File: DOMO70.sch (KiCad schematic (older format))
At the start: 3 parts

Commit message: Layed down groundwork for schematic.
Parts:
- added SW? (x2): Rotary_Encoder_Switch, symbol Device:Rotary_Encoder_Switch
- added U?: OLED-SSD1306-OLED-SSD1306-4pin-128x32, symbol OLED-SSD1306-4pin-128x32:OLED-SSD1306-OLED-SSD1306-4pin-128x32
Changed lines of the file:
@@
 EESchema Schematic File Version 4
+LIBS:DOMO70-cache
 EELAYER 30 0
 EELAYER END
@@
 	1    0    0    -1
 $EndComp
+$Comp
+L OLED-SSD1306-4pin-128x32:OLED-SSD1306-OLED-SSD1306-4pin-128x32 U?
+U 1 1 5DFD98F6
+P 5700 4850
+F 0 "U?" H 5617 5225 50  0000 C CNN
+F 1 "OLED-SSD1306-OLED-SSD1306-4pin-128x32" H 5617 5134 50  0000 C CNN
+F 2 "" H 5700 5250 50  0001 C CNN
+F 3 "" H 5700 5250 50  0001 C CNN
+	1    5700 4850
+	1    0    0    -1
+$EndComp
+$Comp
+L Device:Rotary_Encoder_Switch SW?
+U 1 1 5DFDA3D1
+P 3750 3250
+F 0 "SW?" H 3750 3617 50  0000 C CNN
+F 1 "Rotary_Encoder_Switch" H 3750 3526 50  0000 C CNN
+F 2 "" H 3600 3410 50  0001 C CNN
+F 3 "~" H 3750 3510 50  0001 C CNN
+	1    3750 3250
+	1    0    0    -1
+$EndComp
+$Comp
+L Device:Rotary_Encoder_Switch SW?
+U 1 1 5DFDAD55
+P 4700 3300
+F 0 "SW?" H 4700 3667 50  0000 C CNN
+F 1 "Rotary_Encoder_Switch" H 4700 3576 50  0000 C CNN
+F 2 "" H 4550 3460 50  0001 C CNN
+F 3 "~" H 4700 3560 50  0001 C CNN
+	1    4700 3300
+	1    0    0    -1
+$EndComp

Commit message: First Real Schematic
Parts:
- added D10, D11, D12, D13, D14, D15, D16, D17, D18, D19, D2, D20, D21, D22, D23, D24, D25, D26, D27, D28, D29, D3, D30, D31, D32, D33, D34, D35, D36, D37, D38, D39, D4, D40, D41, D42, D43, D44, D45, D46, D47, D48, D49, D5, D50, D51, D52, D53, D54, D55, D56, D57, D58, D59, D6, D60, D61, D62, D63, D64, D65, D66, D67, D68, D69, D7, D70, D8, D9: 1N4148, Diode_THT:D_DO-35_SOD27_P7.62mm_Horizontal, symbol Diode:1N4148
- added MX10, MX11, MX12, MX13, MX14, MX15, MX16, MX17, MX18, MX19, MX2, MX20, MX21, MX22, MX23, MX24, MX25, MX26, MX27, MX28, MX29, MX3, MX30, MX31, MX32, MX33, MX34, MX35, MX36, MX37, MX38, MX39, MX4, MX40, MX41, MX42, MX43, MX44, MX45, MX46, MX47, MX48, MX49, MX5, MX50, MX51, MX52, MX53, MX54, MX55, MX56, MX57, MX58, MX59, MX6, MX60, MX61, MX62, MX63, MX64, MX65, MX66, MX67, MX68, MX69, MX7, MX70, MX8, MX9: MX-NoLED, symbol MX_Alps_Hybrid:MX-NoLED
- gave numbers to parts that had none: 6
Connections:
- net COL0: now reaches MX1.1 (COL)
- net COL0: now also U2.B11 (PB11), MX2.1 (COL), MX3.1 (COL), MX4.1 (COL), MX5.1 (COL), MX6.1 (COL), MX7.1 (COL), MX8.1 (COL), MX9.1 (COL)
- net at MX1.2 (ROW): now also D1.2 (A)
- net SDA: now reaches U1.1 (SDA)
- net SDA: now also U2.B7 (PB7/SDA)
- net SCL: now reaches U1.2 (SCL)
- net SCL: now also U2.B6 (PB6/SCL)
- net VCC: now reaches U1.3 (VCC)
- net VCC: now also U2.3.3V (VCC/3.3v)
- net GND: now reaches U1.4 (GND)
- net GND: now also SW1.C, SW2.C, U2.GND
- net ROW0: now reaches D1.1 (K)
- net ROW0: now also U2.A2 (PA2), D10.1 (K), D19.1 (K), D28.1 (K), D37.1 (K), D46.1 (K), D55.1 (K), D64.1 (K)
- net ENC1A: now reaches SW1.A
- net ENC1A: now also U2.B0 (PB0)
- net ENC1B: now reaches SW1.B
- net ENC1B: now also U2.B1 (PB1)
- net ROW7: now reaches SW1.S1
- net ROW7: now also U2.B9 (PB9), D17.1 (K), D26.1 (K), D35.1 (K), D44.1 (K), D53.1 (K), D62.1 (K), D8.1 (K)
- net COL7: now reaches SW1.S2
- net COL7: now also SW2.S2, U2.B2 (PB2), MX64.1 (COL), MX65.1 (COL), MX66.1 (COL), MX67.1 (COL), MX68.1 (COL), MX69.1 (COL), MX70.1 (COL)
- net ENC2A: now reaches SW2.A
- net ENC2A: now also U2.A7 (PA7)
- net ENC2B: now reaches SW2.B
- net ENC2B: now also U2.A6 (PA6)
- net ROW8: now reaches SW2.S1
- net ROW8: now also U2.B10 (PB10), D18.1 (K), D27.1 (K), D36.1 (K), D45.1 (K), D54.1 (K), D63.1 (K), D9.1 (K)
- net ROW2: now reaches U2.A0 (PA0)
- net ROW2: now also D12.1 (K), D21.1 (K), D3.1 (K), D30.1 (K), D39.1 (K), D48.1 (K), D57.1 (K), D66.1 (K)
- net ROW1: now reaches U2.A1 (PA1)
- net ROW1: now also D11.1 (K), D2.1 (K), D20.1 (K), D29.1 (K), D38.1 (K), D47.1 (K), D56.1 (K), D65.1 (K)
- net COL3: now reaches U2.A13 (PA13/SWDIO)
- net COL3: now also MX28.1 (COL), MX29.1 (COL), MX30.1 (COL), MX31.1 (COL), MX32.1 (COL), MX33.1 (COL), MX34.1 (COL), MX35.1 (COL), MX36.1 (COL)
- net COL2: now reaches U2.A14 (PA14/SWCLK)
- net COL2: now also MX19.1 (COL), MX20.1 (COL), MX21.1 (COL), MX22.1 (COL), MX23.1 (COL), MX24.1 (COL), MX25.1 (COL), MX26.1 (COL), MX27.1 (COL)
- net COL1: now reaches U2.B12 (PB12)
- net COL1: now also MX10.1 (COL), MX11.1 (COL), MX12.1 (COL), MX13.1 (COL), MX14.1 (COL), MX15.1 (COL), MX16.1 (COL), MX17.1 (COL), MX18.1 (COL)
- net ROW4: now reaches U2.B13 (PB13/SCLK)
- net ROW4: now also D14.1 (K), D23.1 (K), D32.1 (K), D41.1 (K), D5.1 (K), D50.1 (K), D59.1 (K), D68.1 (K)
- net ROW5: now reaches U2.B14 (PB14/MISO)
- net ROW5: now also D15.1 (K), D24.1 (K), D33.1 (K), D42.1 (K), D51.1 (K), D6.1 (K), D60.1 (K), D69.1 (K)
- net ROW6: now reaches U2.B15 (PB15/MOSI)
- net ROW6: now also D16.1 (K), D25.1 (K), D34.1 (K), D43.1 (K), D52.1 (K), D61.1 (K), D7.1 (K), D70.1 (K)
- net COL6: now reaches U2.B3 (PB3)
- net COL6: now also MX55.1 (COL), MX56.1 (COL), MX57.1 (COL), MX58.1 (COL), MX59.1 (COL), MX60.1 (COL), MX61.1 (COL), MX62.1 (COL), MX63.1 (COL)
- net COL5: now reaches U2.B4 (PB4)
- net COL5: now also MX46.1 (COL), MX47.1 (COL), MX48.1 (COL), MX49.1 (COL), MX50.1 (COL), MX51.1 (COL), MX52.1 (COL), MX53.1 (COL), MX54.1 (COL)
- net COL4: now reaches U2.B5 (PB5)
- net COL4: now also MX37.1 (COL), MX38.1 (COL), MX39.1 (COL), MX40.1 (COL), MX41.1 (COL), MX42.1 (COL), MX43.1 (COL), MX44.1 (COL), MX45.1 (COL)
- net ROW3: now reaches U2.B8 (PB8)
- net ROW3: now also D13.1 (K), D22.1 (K), D31.1 (K), D4.1 (K), D40.1 (K), D49.1 (K), D58.1 (K), D67.1 (K)
- new net: D10.2 (A), MX10.2 (ROW)
- new net: D2.2 (A), MX2.2 (ROW)
- new net: D11.2 (A), MX11.2 (ROW)
- new net: D19.2 (A), MX19.2 (ROW)
- new net: D28.2 (A), MX28.2 (ROW)
- new net: D20.2 (A), MX20.2 (ROW)
- new net: D29.2 (A), MX29.2 (ROW)
- new net: D3.2 (A), MX3.2 (ROW)
- new net: D12.2 (A), MX12.2 (ROW)
- new net: D4.2 (A), MX4.2 (ROW)
- new net: D13.2 (A), MX13.2 (ROW)
- new net: D21.2 (A), MX21.2 (ROW)
- new net: D30.2 (A), MX30.2 (ROW)
- new net: D22.2 (A), MX22.2 (ROW)
- new net: D31.2 (A), MX31.2 (ROW)
- new net: D5.2 (A), MX5.2 (ROW)
- new net: D14.2 (A), MX14.2 (ROW)
- new net: D23.2 (A), MX23.2 (ROW)
- new net: D32.2 (A), MX32.2 (ROW)
- new net: D37.2 (A), MX37.2 (ROW)
- new net: D46.2 (A), MX46.2 (ROW)
- new net: D38.2 (A), MX38.2 (ROW)
- new net: D47.2 (A), MX47.2 (ROW)
- new net: D55.2 (A), MX55.2 (ROW)
- new net: D64.2 (A), MX64.2 (ROW)
- new net: D56.2 (A), MX56.2 (ROW)
- new net: D65.2 (A), MX65.2 (ROW)
- new net: D39.2 (A), MX39.2 (ROW)
- new net: D48.2 (A), MX48.2 (ROW)
- new net: D40.2 (A), MX40.2 (ROW)
- new net: D49.2 (A), MX49.2 (ROW)
- new net: D57.2 (A), MX57.2 (ROW)
- new net: D66.2 (A), MX66.2 (ROW)
- new net: D58.2 (A), MX58.2 (ROW)
- new net: D67.2 (A), MX67.2 (ROW)
- new net: D41.2 (A), MX41.2 (ROW)
- new net: D50.2 (A), MX50.2 (ROW)
- new net: D59.2 (A), MX59.2 (ROW)
- new net: D68.2 (A), MX68.2 (ROW)
- new net: D6.2 (A), MX6.2 (ROW)
- new net: D15.2 (A), MX15.2 (ROW)
- new net: D7.2 (A), MX7.2 (ROW)
- new net: D16.2 (A), MX16.2 (ROW)
- new net: D24.2 (A), MX24.2 (ROW)
- new net: D33.2 (A), MX33.2 (ROW)
- new net: D25.2 (A), MX25.2 (ROW)
- new net: D34.2 (A), MX34.2 (ROW)
- new net: D8.2 (A), MX8.2 (ROW)
- new net: D17.2 (A), MX17.2 (ROW)
- new net: D9.2 (A), MX9.2 (ROW)
- new net: D18.2 (A), MX18.2 (ROW)
- new net: D26.2 (A), MX26.2 (ROW)
- new net: D35.2 (A), MX35.2 (ROW)
- new net: D27.2 (A), MX27.2 (ROW)
- new net: D36.2 (A), MX36.2 (ROW)
- new net: D42.2 (A), MX42.2 (ROW)
- new net: D51.2 (A), MX51.2 (ROW)
- new net: D43.2 (A), MX43.2 (ROW)
- new net: D52.2 (A), MX52.2 (ROW)
- new net: D60.2 (A), MX60.2 (ROW)
- new net: D61.2 (A), MX61.2 (ROW)
- new net: D69.2 (A), MX69.2 (ROW)
- new net: D44.2 (A), MX44.2 (ROW)
- new net: D53.2 (A), MX53.2 (ROW)
- new net: D45.2 (A), MX45.2 (ROW)
- new net: D54.2 (A), MX54.2 (ROW)
- new net: D62.2 (A), MX62.2 (ROW)
- new net: D70.2 (A), MX70.2 (ROW)
- new net: D63.2 (A), MX63.2 (ROW)
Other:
- moved on the sheet: D1, MX1, SW1, SW2, U1, U2

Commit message: Messing with matrix
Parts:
- removed D53: 1N4148, Diode_THT:D_DO-35_SOD27_P7.62mm_Horizontal, symbol Diode:1N4148
- removed MX53: MX-NoLED, symbol MX_Alps_Hybrid:MX-NoLED
- added D? (x5): 1N4148, cftkb:D_DO-35_SOD27_P5.08mm_Horizontal, symbol Diode:1N4148
- added MX? (x3): MX-NoLED, MX_Only:MXOnly-1U-NoLED, symbol MX_Alps_Hybrid:MX-NoLED
- D?: renamed from D1; footprint Diode_THT:D_DO-35_SOD27_P7.62mm_Horizontal -> cftkb:D_DO-35_SOD27_P5.08mm_Horizontal
- D?: renamed from D10; footprint Diode_THT:D_DO-35_SOD27_P7.62mm_Horizontal -> cftkb:D_DO-35_SOD27_P5.08mm_Horizontal
- D?: renamed from D2; footprint Diode_THT:D_DO-35_SOD27_P7.62mm_Horizontal -> cftkb:D_DO-35_SOD27_P5.08mm_Horizontal
- D?: renamed from D11; footprint Diode_THT:D_DO-35_SOD27_P7.62mm_Horizontal -> cftkb:D_DO-35_SOD27_P5.08mm_Horizontal
- D?: renamed from D19; footprint Diode_THT:D_DO-35_SOD27_P7.62mm_Horizontal -> cftkb:D_DO-35_SOD27_P5.08mm_Horizontal
- D?: renamed from D28; footprint Diode_THT:D_DO-35_SOD27_P7.62mm_Horizontal -> cftkb:D_DO-35_SOD27_P5.08mm_Horizontal
- D?: renamed from D20; footprint Diode_THT:D_DO-35_SOD27_P7.62mm_Horizontal -> cftkb:D_DO-35_SOD27_P5.08mm_Horizontal
- D?: renamed from D29; footprint Diode_THT:D_DO-35_SOD27_P7.62mm_Horizontal -> cftkb:D_DO-35_SOD27_P5.08mm_Horizontal
- D?: renamed from D3; footprint Diode_THT:D_DO-35_SOD27_P7.62mm_Horizontal -> cftkb:D_DO-35_SOD27_P5.08mm_Horizontal
- D?: renamed from D12; footprint Diode_THT:D_DO-35_SOD27_P7.62mm_Horizontal -> cftkb:D_DO-35_SOD27_P5.08mm_Horizontal
- D?: renamed from D4; footprint Diode_THT:D_DO-35_SOD27_P7.62mm_Horizontal -> cftkb:D_DO-35_SOD27_P5.08mm_Horizontal
- D?: renamed from D13; footprint Diode_THT:D_DO-35_SOD27_P7.62mm_Horizontal -> cftkb:D_DO-35_SOD27_P5.08mm_Horizontal
- D?: renamed from D21; footprint Diode_THT:D_DO-35_SOD27_P7.62mm_Horizontal -> cftkb:D_DO-35_SOD27_P5.08mm_Horizontal
- D?: renamed from D30; footprint Diode_THT:D_DO-35_SOD27_P7.62mm_Horizontal -> cftkb:D_DO-35_SOD27_P5.08mm_Horizontal
- D?: renamed from D22; footprint Diode_THT:D_DO-35_SOD27_P7.62mm_Horizontal -> cftkb:D_DO-35_SOD27_P5.08mm_Horizontal
- D?: renamed from D31; footprint Diode_THT:D_DO-35_SOD27_P7.62mm_Horizontal -> cftkb:D_DO-35_SOD27_P5.08mm_Horizontal
- D?: renamed from D5; footprint Diode_THT:D_DO-35_SOD27_P7.62mm_Horizontal -> cftkb:D_DO-35_SOD27_P5.08mm_Horizontal
- D?: renamed from D14; footprint Diode_THT:D_DO-35_SOD27_P7.62mm_Horizontal -> cftkb:D_DO-35_SOD27_P5.08mm_Horizontal
- D?: renamed from D23; footprint Diode_THT:D_DO-35_SOD27_P7.62mm_Horizontal -> cftkb:D_DO-35_SOD27_P5.08mm_Horizontal
- D?: renamed from D32; footprint Diode_THT:D_DO-35_SOD27_P7.62mm_Horizontal -> cftkb:D_DO-35_SOD27_P5.08mm_Horizontal
- D?: renamed from D37; footprint Diode_THT:D_DO-35_SOD27_P7.62mm_Horizontal -> cftkb:D_DO-35_SOD27_P5.08mm_Horizontal
- D?: renamed from D46; footprint Diode_THT:D_DO-35_SOD27_P7.62mm_Horizontal -> cftkb:D_DO-35_SOD27_P5.08mm_Horizontal
- D?: renamed from D38; footprint Diode_THT:D_DO-35_SOD27_P7.62mm_Horizontal -> cftkb:D_DO-35_SOD27_P5.08mm_Horizontal
- D?: renamed from D47; footprint Diode_THT:D_DO-35_SOD27_P7.62mm_Horizontal -> cftkb:D_DO-35_SOD27_P5.08mm_Horizontal
- D?: renamed from D55; footprint Diode_THT:D_DO-35_SOD27_P7.62mm_Horizontal -> cftkb:D_DO-35_SOD27_P5.08mm_Horizontal
- D?: renamed from D64; footprint Diode_THT:D_DO-35_SOD27_P7.62mm_Horizontal -> cftkb:D_DO-35_SOD27_P5.08mm_Horizontal
- D?: renamed from D56; footprint Diode_THT:D_DO-35_SOD27_P7.62mm_Horizontal -> cftkb:D_DO-35_SOD27_P5.08mm_Horizontal
- D?: renamed from D65; footprint Diode_THT:D_DO-35_SOD27_P7.62mm_Horizontal -> cftkb:D_DO-35_SOD27_P5.08mm_Horizontal
- D?: renamed from D39; footprint Diode_THT:D_DO-35_SOD27_P7.62mm_Horizontal -> cftkb:D_DO-35_SOD27_P5.08mm_Horizontal
- D?: renamed from D48; footprint Diode_THT:D_DO-35_SOD27_P7.62mm_Horizontal -> cftkb:D_DO-35_SOD27_P5.08mm_Horizontal
- D?: renamed from D40; footprint Diode_THT:D_DO-35_SOD27_P7.62mm_Horizontal -> cftkb:D_DO-35_SOD27_P5.08mm_Horizontal
- D?: renamed from D49; footprint Diode_THT:D_DO-35_SOD27_P7.62mm_Horizontal -> cftkb:D_DO-35_SOD27_P5.08mm_Horizontal
- D?: renamed from D57; footprint Diode_THT:D_DO-35_SOD27_P7.62mm_Horizontal -> cftkb:D_DO-35_SOD27_P5.08mm_Horizontal
- D?: renamed from D66; footprint Diode_THT:D_DO-35_SOD27_P7.62mm_Horizontal -> cftkb:D_DO-35_SOD27_P5.08mm_Horizontal
- D?: renamed from D58; footprint Diode_THT:D_DO-35_SOD27_P7.62mm_Horizontal -> cftkb:D_DO-35_SOD27_P5.08mm_Horizontal
- D?: renamed from D67; footprint Diode_THT:D_DO-35_SOD27_P7.62mm_Horizontal -> cftkb:D_DO-35_SOD27_P5.08mm_Horizontal
- D?: renamed from D41; footprint Diode_THT:D_DO-35_SOD27_P7.62mm_Horizontal -> cftkb:D_DO-35_SOD27_P5.08mm_Horizontal
- D?: renamed from D50; footprint Diode_THT:D_DO-35_SOD27_P7.62mm_Horizontal -> cftkb:D_DO-35_SOD27_P5.08mm_Horizontal
- D?: renamed from D59; footprint Diode_THT:D_DO-35_SOD27_P7.62mm_Horizontal -> cftkb:D_DO-35_SOD27_P5.08mm_Horizontal
- D?: renamed from D68; footprint Diode_THT:D_DO-35_SOD27_P7.62mm_Horizontal -> cftkb:D_DO-35_SOD27_P5.08mm_Horizontal
- D?: renamed from D6; footprint Diode_THT:D_DO-35_SOD27_P7.62mm_Horizontal -> cftkb:D_DO-35_SOD27_P5.08mm_Horizontal
- D?: renamed from D15; footprint Diode_THT:D_DO-35_SOD27_P7.62mm_Horizontal -> cftkb:D_DO-35_SOD27_P5.08mm_Horizontal
- D?: renamed from D7; footprint Diode_THT:D_DO-35_SOD27_P7.62mm_Horizontal -> cftkb:D_DO-35_SOD27_P5.08mm_Horizontal
- D?: renamed from D16; footprint Diode_THT:D_DO-35_SOD27_P7.62mm_Horizontal -> cftkb:D_DO-35_SOD27_P5.08mm_Horizontal
- D?: renamed from D24; footprint Diode_THT:D_DO-35_SOD27_P7.62mm_Horizontal -> cftkb:D_DO-35_SOD27_P5.08mm_Horizontal
- D?: renamed from D33; footprint Diode_THT:D_DO-35_SOD27_P7.62mm_Horizontal -> cftkb:D_DO-35_SOD27_P5.08mm_Horizontal
- D?: renamed from D25; footprint Diode_THT:D_DO-35_SOD27_P7.62mm_Horizontal -> cftkb:D_DO-35_SOD27_P5.08mm_Horizontal
- D?: renamed from D34; footprint Diode_THT:D_DO-35_SOD27_P7.62mm_Horizontal -> cftkb:D_DO-35_SOD27_P5.08mm_Horizontal
- D?: renamed from D8; footprint Diode_THT:D_DO-35_SOD27_P7.62mm_Horizontal -> cftkb:D_DO-35_SOD27_P5.08mm_Horizontal
- D?: renamed from D17; footprint Diode_THT:D_DO-35_SOD27_P7.62mm_Horizontal -> cftkb:D_DO-35_SOD27_P5.08mm_Horizontal
- D?: renamed from D9; footprint Diode_THT:D_DO-35_SOD27_P7.62mm_Horizontal -> cftkb:D_DO-35_SOD27_P5.08mm_Horizontal
- D?: renamed from D18; footprint Diode_THT:D_DO-35_SOD27_P7.62mm_Horizontal -> cftkb:D_DO-35_SOD27_P5.08mm_Horizontal
- D?: renamed from D26; footprint Diode_THT:D_DO-35_SOD27_P7.62mm_Horizontal -> cftkb:D_DO-35_SOD27_P5.08mm_Horizontal
- D?: renamed from D35; footprint Diode_THT:D_DO-35_SOD27_P7.62mm_Horizontal -> cftkb:D_DO-35_SOD27_P5.08mm_Horizontal
- D?: renamed from D27; footprint Diode_THT:D_DO-35_SOD27_P7.62mm_Horizontal -> cftkb:D_DO-35_SOD27_P5.08mm_Horizontal
- D?: renamed from D36; footprint Diode_THT:D_DO-35_SOD27_P7.62mm_Horizontal -> cftkb:D_DO-35_SOD27_P5.08mm_Horizontal
- D?: renamed from D42; footprint Diode_THT:D_DO-35_SOD27_P7.62mm_Horizontal -> cftkb:D_DO-35_SOD27_P5.08mm_Horizontal
- D?: renamed from D51; footprint Diode_THT:D_DO-35_SOD27_P7.62mm_Horizontal -> cftkb:D_DO-35_SOD27_P5.08mm_Horizontal
- D?: renamed from D43; footprint Diode_THT:D_DO-35_SOD27_P7.62mm_Horizontal -> cftkb:D_DO-35_SOD27_P5.08mm_Horizontal
- D?: renamed from D52; footprint Diode_THT:D_DO-35_SOD27_P7.62mm_Horizontal -> cftkb:D_DO-35_SOD27_P5.08mm_Horizontal
- D?: renamed from D60; footprint Diode_THT:D_DO-35_SOD27_P7.62mm_Horizontal -> cftkb:D_DO-35_SOD27_P5.08mm_Horizontal
- D?: renamed from D61; footprint Diode_THT:D_DO-35_SOD27_P7.62mm_Horizontal -> cftkb:D_DO-35_SOD27_P5.08mm_Horizontal
- D?: renamed from D69; footprint Diode_THT:D_DO-35_SOD27_P7.62mm_Horizontal -> cftkb:D_DO-35_SOD27_P5.08mm_Horizontal
- D?: renamed from D44; footprint Diode_THT:D_DO-35_SOD27_P7.62mm_Horizontal -> cftkb:D_DO-35_SOD27_P5.08mm_Horizontal
- D?: renamed from D45; footprint Diode_THT:D_DO-35_SOD27_P7.62mm_Horizontal -> cftkb:D_DO-35_SOD27_P5.08mm_Horizontal
- D?: renamed from D54; footprint Diode_THT:D_DO-35_SOD27_P7.62mm_Horizontal -> cftkb:D_DO-35_SOD27_P5.08mm_Horizontal
- D?: renamed from D62; footprint Diode_THT:D_DO-35_SOD27_P7.62mm_Horizontal -> cftkb:D_DO-35_SOD27_P5.08mm_Horizontal
- D?: renamed from D70; footprint Diode_THT:D_DO-35_SOD27_P7.62mm_Horizontal -> cftkb:D_DO-35_SOD27_P5.08mm_Horizontal
- D?: renamed from D63; footprint Diode_THT:D_DO-35_SOD27_P7.62mm_Horizontal -> cftkb:D_DO-35_SOD27_P5.08mm_Horizontal
- MX?: renamed from MX1; footprint (none) -> MX_Only:MXOnly-1U-NoLED
- MX?: renamed from MX10; footprint (none) -> MX_Only:MXOnly-1U-NoLED
- MX?: renamed from MX2; footprint (none) -> MX_Only:MXOnly-1.5U-NoLED
- MX?: renamed from MX11; footprint (none) -> MX_Only:MXOnly-1U-NoLED
- MX?: renamed from MX19; footprint (none) -> MX_Only:MXOnly-1U-NoLED
- MX?: renamed from MX28; footprint (none) -> MX_Only:MXOnly-1U-NoLED
- MX?: renamed from MX20; footprint (none) -> MX_Only:MXOnly-1U-NoLED
- MX?: renamed from MX29; footprint (none) -> MX_Only:MXOnly-1U-NoLED
- MX?: renamed from MX3; footprint (none) -> MX_Only:MXOnly-1U-NoLED
- MX?: renamed from MX12; footprint (none) -> MX_Only:MXOnly-1U-NoLED
- MX?: renamed from MX4; footprint (none) -> MX_Only:MXOnly-1U-NoLED
- MX?: renamed from MX13; footprint (none) -> MX_Only:MXOnly-1U-NoLED
- MX?: renamed from MX21; footprint (none) -> MX_Only:MXOnly-1U-NoLED
- MX?: renamed from MX30; footprint (none) -> MX_Only:MXOnly-1U-NoLED
- MX?: renamed from MX22; footprint (none) -> MX_Only:MXOnly-1U-NoLED
- MX?: renamed from MX31; footprint (none) -> MX_Only:MXOnly-1U-NoLED
- MX?: renamed from MX5; footprint (none) -> MX_Only:MXOnly-1U-NoLED
- MX?: renamed from MX14; footprint (none) -> MX_Only:MXOnly-1U-NoLED
- MX?: renamed from MX23; footprint (none) -> MX_Only:MXOnly-1U-NoLED
- MX?: renamed from MX32; footprint (none) -> MX_Only:MXOnly-1U-NoLED
- MX?: renamed from MX37; footprint (none) -> MX_Only:MXOnly-1U-NoLED
- MX?: renamed from MX46; footprint (none) -> MX_Only:MXOnly-1U-NoLED
- MX?: renamed from MX38; footprint (none) -> MX_Only:MXOnly-1U-NoLED
- MX?: renamed from MX47; footprint (none) -> MX_Only:MXOnly-1U-NoLED
- MX?: renamed from MX55; footprint (none) -> MX_Only:MXOnly-1U-NoLED
- MX?: renamed from MX64; footprint (none) -> MX_Only:MXOnly-1U-NoLED
- MX?: renamed from MX56; footprint (none) -> MX_Only:MXOnly-1U-NoLED
- MX?: renamed from MX65; footprint (none) -> MX_Only:MXOnly-1U-NoLED
- MX?: renamed from MX39; footprint (none) -> MX_Only:MXOnly-1U-NoLED
- MX?: renamed from MX48; footprint (none) -> MX_Only:MXOnly-1U-NoLED
- MX?: renamed from MX40; footprint (none) -> MX_Only:MXOnly-1U-NoLED
- MX?: renamed from MX49; footprint (none) -> MX_Only:MXOnly-1U-NoLED
- MX?: renamed from MX57; footprint (none) -> MX_Only:MXOnly-1U-NoLED
- MX?: renamed from MX66; footprint (none) -> MX_Only:MXOnly-1U-NoLED
- MX?: renamed from MX58; footprint (none) -> MX_Only:MXOnly-1U-NoLED
- MX?: renamed from MX67; footprint (none) -> MX_Only:MXOnly-1U-NoLED
- MX?: renamed from MX41; footprint (none) -> MX_Only:MXOnly-1U-NoLED
- MX?: renamed from MX50; footprint (none) -> MX_Only:MXOnly-1U-NoLED
- MX?: renamed from MX59; footprint (none) -> MX_Only:MXOnly-1U-NoLED
- MX?: renamed from MX68; footprint (none) -> MX_Only:MXOnly-1U-NoLED
- MX?: renamed from MX6; footprint (none) -> MX_Only:MXOnly-1U-NoLED
- MX?: renamed from MX15; footprint (none) -> MX_Only:MXOnly-1U-NoLED
- MX?: renamed from MX7; footprint (none) -> MX_Only:MXOnly-1U-NoLED
- MX?: renamed from MX16; footprint (none) -> MX_Only:MXOnly-1U-NoLED
- MX?: renamed from MX24; footprint (none) -> MX_Only:MXOnly-1U-NoLED
- MX?: renamed from MX33; footprint (none) -> MX_Only:MXOnly-1U-NoLED
- MX?: renamed from MX25; footprint (none) -> MX_Only:MXOnly-1U-NoLED
- MX?: renamed from MX34; footprint (none) -> MX_Only:MXOnly-1U-NoLED
- MX?: renamed from MX8; footprint (none) -> MX_Only:MXOnly-1U-NoLED
- MX?: renamed from MX17; footprint (none) -> MX_Only:MXOnly-1U-NoLED
- MX?: renamed from MX9; footprint (none) -> MX_Only:MXOnly-1U-NoLED
- MX?: renamed from MX18; footprint (none) -> MX_Only:MXOnly-1U-NoLED
- MX?: renamed from MX26; footprint (none) -> MX_Only:MXOnly-1U-NoLED
- MX?: renamed from MX35; footprint (none) -> MX_Only:MXOnly-1U-NoLED
- MX?: renamed from MX27; footprint (none) -> MX_Only:MXOnly-1U-NoLED
- MX?: renamed from MX36; footprint (none) -> MX_Only:MXOnly-1U-NoLED
- MX?: renamed from MX42; footprint (none) -> MX_Only:MXOnly-1U-NoLED
- MX?: renamed from MX51; footprint (none) -> MX_Only:MXOnly-1U-NoLED
- MX?: renamed from MX43; footprint (none) -> MX_Only:MXOnly-1U-NoLED
- MX?: renamed from MX52; footprint (none) -> MX_Only:MXOnly-1U-NoLED
- MX?: renamed from MX60; footprint (none) -> MX_Only:MXOnly-1U-NoLED
- MX?: renamed from MX61; footprint (none) -> MX_Only:MXOnly-1U-NoLED
- MX?: renamed from MX69; footprint (none) -> MX_Only:MXOnly-1U-NoLED
- MX?: renamed from MX44; footprint (none) -> MX_Only:MXOnly-1U-NoLED
- MX?: renamed from MX45; footprint (none) -> MX_Only:MXOnly-1U-NoLED
- MX?: renamed from MX54; footprint (none) -> MX_Only:MXOnly-1U-NoLED
- MX?: renamed from MX62; footprint (none) -> MX_Only:MXOnly-1U-NoLED
- MX?: renamed from MX70; footprint (none) -> MX_Only:MXOnly-1U-NoLED
- MX?: renamed from MX63; footprint (none) -> MX_Only:MXOnly-1U-NoLED
- SW?: renamed from SW1; footprint (none) -> Rotary_Encoder:RotaryEncoder_Alps_EC11E-Switch_Vertical_H20mm
- SW?: renamed from SW2; footprint (none) -> Rotary_Encoder:RotaryEncoder_Alps_EC11E-Switch_Vertical_H20mm
- U?: renamed from U1; footprint (none) -> OLED-SSD1306-4pin-128x32:OLED-1306-Supports
- U?: renamed from U2; footprint (none) -> proton_c:proton_c
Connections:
- net COL0: now also U?.B14 (PB14/MISO); no longer MX?.1 (COL), MX?.1 (COL), MX?.1 (COL), MX?.1 (COL), U?.B11 (PB11)
- net COL1: now also U?.B15 (PB15/MOSI); no longer MX?.1 (COL), MX?.1 (COL), MX?.1 (COL), MX?.1 (COL), U?.B12 (PB12)
- net COL2: now also U?.B9 (PB9); no longer MX?.1 (COL), MX?.1 (COL), MX?.1 (COL), MX?.1 (COL), U?.A14 (PA14/SWCLK)
- net COL3: now also U?.B10 (PB10); no longer MX?.1 (COL), MX?.1 (COL), MX?.1 (COL), MX?.1 (COL), U?.A13 (PA13/SWDIO)
- net COL4: now also MX?.1 (COL), U?.B11 (PB11); no longer MX?.1 (COL), MX?.1 (COL), MX?.1 (COL), MX?.1 (COL), MX?.1 (COL), U?.B5 (PB5)
- net COL5: now also MX?.1 (COL), U?.B12 (PB12); no longer MX?.1 (COL), MX?.1 (COL), MX?.1 (COL), MX?.1 (COL), U?.B4 (PB4)
- net COL6: now also MX?.1 (COL), U?.A14 (PA14/SWCLK); no longer MX?.1 (COL), MX?.1 (COL), MX?.1 (COL), MX?.1 (COL), MX?.1 (COL), U?.B3 (PB3)
- net COL7: now also U?.A13 (PA13/SWDIO); no longer MX?.1 (COL), MX?.1 (COL), MX?.1 (COL), SW?.S2, SW?.S2, U?.B2 (PB2)
- net ROW0: now also D?.1 (K), D?.1 (K), D?.1 (K), D?.1 (K), D?.1 (K), D?.1 (K), D?.1 (K)
- net ROW1: now also D?.1 (K), D?.1 (K), D?.1 (K), D?.1 (K), D?.1 (K), D?.1 (K)
- net ROW2: now also D?.1 (K), D?.1 (K), D?.1 (K), D?.1 (K), D?.1 (K)
- net ROW3: now also D?.1 (K), D?.1 (K), D?.1 (K), D?.1 (K), D?.1 (K)
- net ROW4: now also D?.1 (K), D?.1 (K), D?.1 (K), D?.1 (K); no longer D?.1 (K)
- net COL13: now reaches U?.A10 (PA10/RX)
- net COL13: now also MX?.1 (COL), MX?.1 (COL), MX?.1 (COL)
- net COL8: now reaches U?.A8 (PA8)
- net COL8: now also MX?.1 (COL), MX?.1 (COL), MX?.1 (COL), MX?.1 (COL)
- net COL14: now reaches U?.A9 (PA9/TX)
- net COL14: now also MX?.1 (COL), MX?.1 (COL), MX?.1 (COL), MX?.1 (COL)
- removed net ROW5: D?.1 (K), D?.1 (K), D?.1 (K), D?.1 (K), D?.1 (K), D?.1 (K), D?.1 (K), D?.1 (K), U?.B14 (PB14/MISO)
- removed net ROW6: D?.1 (K), D?.1 (K), D?.1 (K), D?.1 (K), D?.1 (K), D?.1 (K), D?.1 (K), D?.1 (K), U?.B15 (PB15/MOSI)
- removed net ROW7: D?.1 (K), D?.1 (K), D?.1 (K), D?.1 (K), D?.1 (K), D?.1 (K), SW?.S1, U?.B9 (PB9)
- removed net ROW8: D?.1 (K), D?.1 (K), D?.1 (K), D?.1 (K), D?.1 (K), D?.1 (K), D?.1 (K), SW?.S1, U?.B10 (PB10)
- new net: D?.2 (A), SW?.S1 (x2)
- new net: MX?.1 (COL), MX?.1 (COL) (x3)
- new net: D?.1 (K), D?.1 (K), D?.1 (K) (x2)
- new net: D?.2 (A), MX?.2 (ROW) (x3)
- new net COL10: MX?.1 (COL), MX?.1 (COL), MX?.1 (COL), MX?.1 (COL), MX?.1 (COL), U?.B3 (PB3)
- new net COL11: MX?.1 (COL), MX?.1 (COL), MX?.1 (COL), MX?.1 (COL), U?.B4 (PB4)
- new net COL12: MX?.1 (COL), MX?.1 (COL), MX?.1 (COL), U?.B5 (PB5)
- new net COL9: MX?.1 (COL), MX?.1 (COL), MX?.1 (COL), MX?.1 (COL), U?.B2 (PB2)
- no-connect marks 0 -> 5
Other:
- moved on the sheet: D?, MX?, SW?, U?

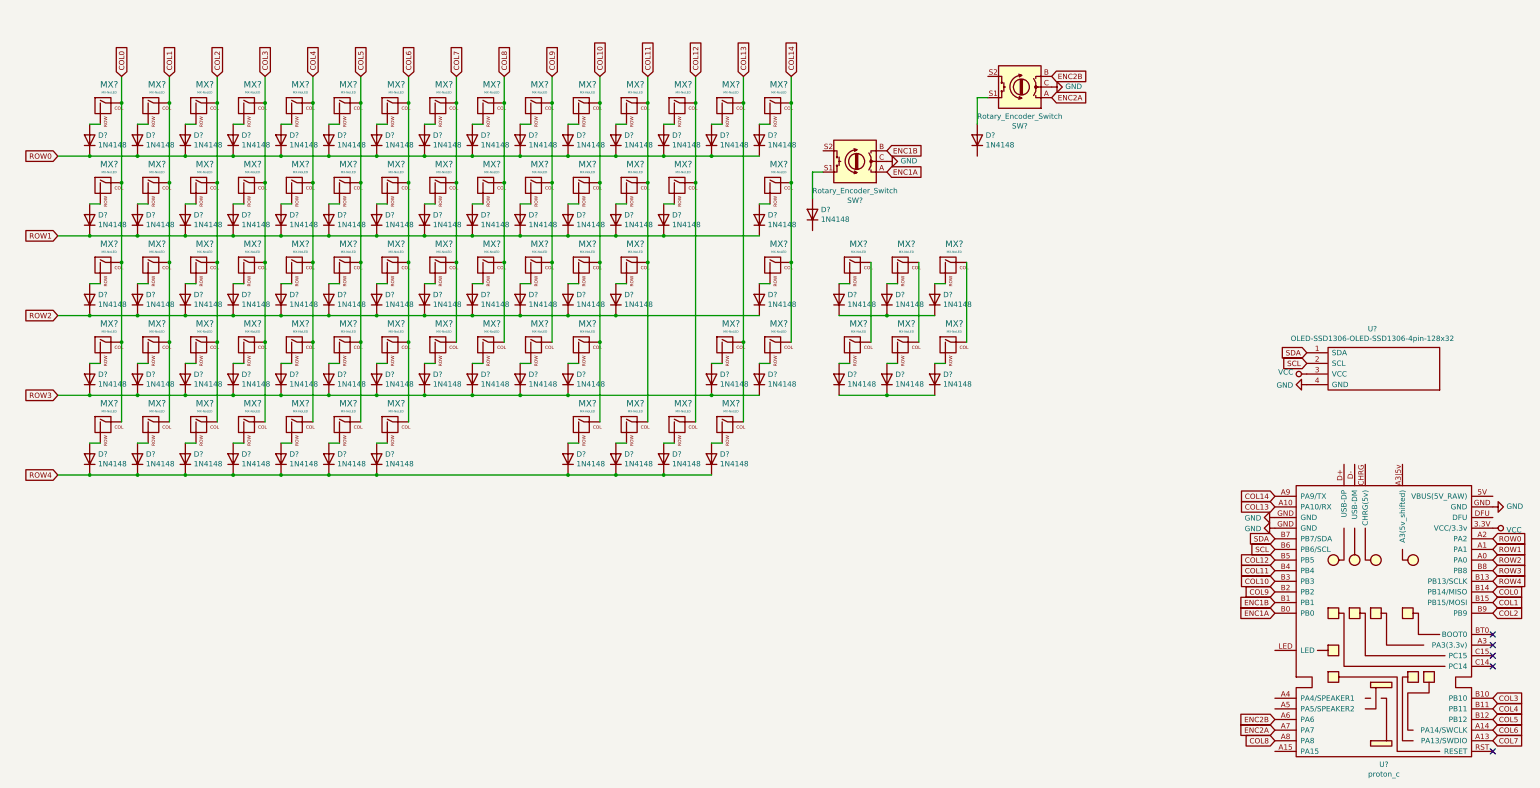
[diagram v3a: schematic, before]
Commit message: Created speaker footprint/symbol
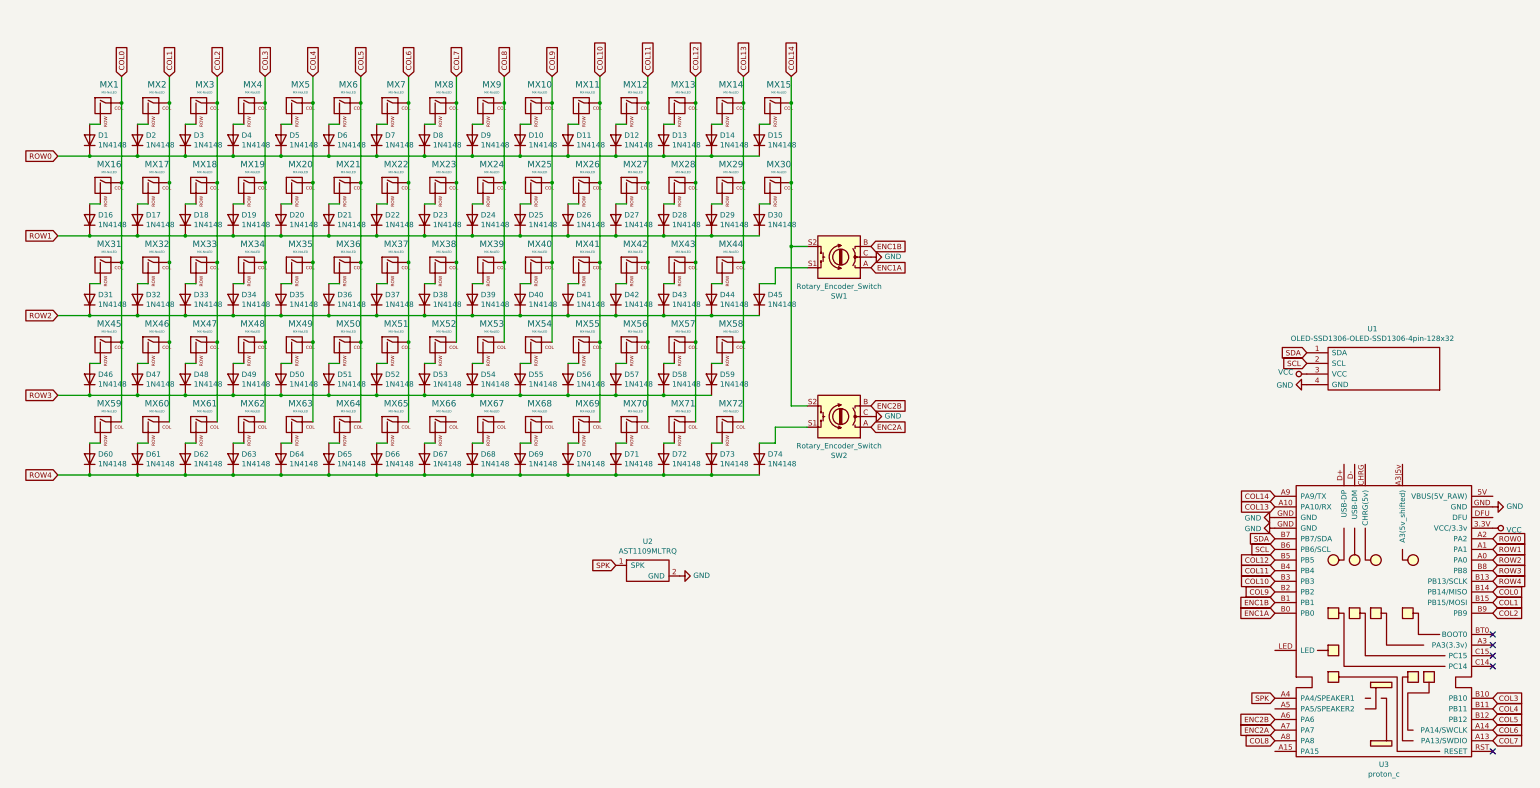
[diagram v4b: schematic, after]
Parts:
- added U2: AST1109MLTRQ, Buzzer_Beeper:Buzzer_Mallory_AST1109MLTRQ, symbol Buzzer_AST1109MLTRQ:AST1109MLTRQ
- gave numbers to parts that had none: 150
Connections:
- net COL11: now also MX56.1 (COL)
- net COL12: now also MX43.1 (COL), MX57.1 (COL)
- net COL13: now also MX29.1 (COL), MX44.1 (COL)
- net COL14: now also SW1.S2, SW2.S2; no longer MX67.1 (COL), MX68.1 (COL)
- net GND: now also U2.2 (GND)
- net ROW1: now also D29.1 (K)
- net ROW2: now also D43.1 (K), D44.1 (K), D45.1 (K); no longer D68.1 (K)
- net ROW3: now also D57.1 (K), D58.1 (K); no longer D69.1 (K)
- net ROW4: now also D67.1 (K), D68.1 (K), D69.1 (K), D74.1 (K)
- net SPK: now reaches U3.A4 (PA4/SPEAKER1)
- net SPK: now also U2.1 (SPK)
- net at MX66.1 (COL): no longer MX56.1 (COL)
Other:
- moved on the sheet: D29, D43, D44, D45, D57, D58, D67, D68, D69, D74, MX29, MX43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

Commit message: Added routing
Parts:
- added MX_14: ExtraMX, MX_Only:MXOnly-2U-NoLED, symbol DomsParts:ExtraMX
- added MX_29: ExtraMX, MX_Only:MXOnly-ISO-ROTATED-ReversedStabilizers-NoLED, symbol DomsParts:ExtraMX
- added MX_31: ExtraMX, MX_Only:MXOnly-1.25U-NoLED, symbol DomsParts:ExtraMX
- added MX_43, MX_60, MX_65: ExtraMX, MX_Only:MXOnly-1U-NoLED, symbol DomsParts:ExtraMX
- added MX_56: ExtraMX, MX_Only:MXOnly-1.75U-NoLED, symbol DomsParts:ExtraMX
- added MX_59, MX_61, MX_64, MX_66: ExtraMX, MX_Only:MXOnly-1.5U-NoLED, symbol DomsParts:ExtraMX
- added MX_62: ExtraMX, MX_Only:MXOnly-7U-ReversedStabilizers-NoLED, symbol DomsParts:ExtraMX
- MX29: footprint MX_Only:MXOnly-1U-NoLED -> MX_Only:MXOnly-1.5U-NoLED
- MX31: footprint MX_Only:MXOnly-1U-NoLED -> MX_Only:MXOnly-1.75U-NoLED
- MX43, MX45: footprint MX_Only:MXOnly-1U-NoLED -> MX_Only:MXOnly-2.25U-NoLED
- MX56: footprint MX_Only:MXOnly-1U-NoLED -> MX_Only:MXOnly-2.75U-NoLED
- MX59, MX60, MX61, MX63, MX64, MX65, MX66: footprint MX_Only:MXOnly-1U-NoLED -> MX_Only:MXOnly-1.25U-NoLED
- MX62: footprint MX_Only:MXOnly-1U-NoLED -> MX_Only:MXOnly-6.25U-ReversedStabilizers-NoLED
- renumbered D46 to D45, D47 to D46, D48 to D47, D49 to D48, D50 to D49, D51 to D50, D52 to D51, D53 to D52, D54 to D53, D55 to D54, D56 to D55, D57 to D56, D58 to D57, D59 to D58, D60 to D59, D61 to D60, D62 to D61, D63 to D62, D64 to D63, D65 to D64, D66 to D65, D67 to D66, D68 to D67, D69 to D68, D70 to D69, D71 to D70, D72 to D71, D73 to D72, D45 to DE1, D74 to DE2, U2 to U1, U3 to U2, U1 to U3
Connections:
- net COL0: now also MX_31.1, MX_59.1
- net COL1: now also MX_60.1
- net COL11: now also MX_56.1
- net COL12: now also MX_43.1
- net COL13: now also MX_14.1, MX_29.1
- net COL2: now also MX_61.1
- net COL3: now also MX_62.1
- net COL5: now also MX_64.1
- net COL6: now also MX_65.1
- net COL7: now also MX66.1 (COL), MX_66.1
- net at D31.2 (A), MX31.2 (ROW): now also MX_31.2
- net at D59.2 (A), MX59.2 (ROW): now also MX_59.2
- net at D60.2 (A), MX60.2 (ROW): now also MX_60.2
- net at D61.2 (A), MX61.2 (ROW): now also MX_61.2
- net at D62.2 (A), MX62.2 (ROW): now also MX_62.2
- net at D64.2 (A), MX64.2 (ROW): now also MX_64.2
- net at D65.2 (A), MX65.2 (ROW): now also MX_65.2
- net at D43.2 (A), MX43.2 (ROW): now also MX_43.2
- net at D14.2 (A), MX14.2 (ROW): now also MX_14.2
- net at D66.2 (A), MX66.2 (ROW): now also MX_66.2
- net at D29.2 (A), MX29.2 (ROW): now also MX_29.2
- net at D56.2 (A), MX56.2 (ROW): now also MX_56.2
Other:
- moved on the sheet: D1, D10, D11, D12, D13, D14, D15, D16, D17, D18, D19, D2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
